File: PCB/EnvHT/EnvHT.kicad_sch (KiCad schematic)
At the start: 21 parts, among them J1 DC, J2 DC, J4 Shelly, U1 LMR16006XDDCR, U4 ESP32-PICO-MINI-02, U7 SHT40

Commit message: Library update
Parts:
- added C5: 10nF, RevK:C_0603, symbol Device:C
- added S1, S2: Screw, RevK:Screw, symbol RevK:Screw
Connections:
- net GND: now also C5.1
- net at R12.2, U4.8 (EN): now also C5.2
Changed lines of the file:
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@@
   (junction (at 197.485 41.275) (diameter 0) (color 0 0 0 0)
+  )
+  (junction (at 40.64 31.75) (diameter 0) (color 0 0 0 0)
   )
   (junction (at 73.66 38.1) (diameter 0) (color 0 0 0 0)
@@
     (pin "1")
     (pin "2")
+  )
+  (symbol (lib_id "Device:C") (at 36.83 31.75 90) (unit 1)
+    (in_bom yes) (on_board yes) (fields_autoplaced)
+    (property "Reference" "C5" (id 0) (at 36.83 25.8912 90))
+    (property "Value" "10nF" (id 1) (at 36.83 28.4281 90))
+    (property "Footprint" "RevK:C_0603" (id 2) (at 40.64 30.7848 0)
+      (effects (font (size 1.27 1.27)) hide)
+    )
+    (property "Datasheet" "~" (id 3) (at 36.83 31.75 0)
+      (effects (font (size 1.27 1.27)) hide)
+    )
+    (pin "1")
+    (pin "2")
+  )
+  (symbol (lib_name "Screw_1") (lib_id "RevK:Screw") (at 266.7 170.18 0) (unit 1)
+    (in_bom no) (on_board yes) (fields_autoplaced)
+    (property "Reference" "S1" (id 0) (at 268.3092 169.3453 0)
+      (effects (font (size 1.27 1.27)) (justify left))
+    )
+    (property "Value" "Screw" (id 1) (at 268.3092 171.8822 0)
+      (effects (font (size 1.27 1.27)) (justify left))
+    )
+    (property "Footprint" "RevK:Screw" (id 2) (at 266.7 170.18 0)
+      (effects (font (size 1.27 1.27)) hide)
+    )
+    (property "Datasheet" "" (id 3) (at 266.7 170.18 0)
+      (effects (font (size 1.27 1.27)) hide)
+    )
   )
   (symbol (lib_id "RevK:Shelly") (at 73.66 40.64 0) (unit 1)
@@
     (pin "2")
   )
+  (symbol (lib_id "power:GND") (at 33.02 31.75 270) (unit 1)
+    (in_bom yes) (on_board yes)
+    (property "Reference" "#PWR0104" (id 0) (at 26.67 31.75 0)
+      (effects (font (size 1.27 1.27)) hide)
+    )
+    (property "Value" "GND" (id 1) (at 29.21 35.56 90)
+      (effects (font (size 1.27 1.27)) (justify left))
+    )
+    (property "Footprint" "" (id 2) (at 33.02 31.75 0)
+      (effects (font (size 1.27 1.27)) hide)
+    )
+    (property "Datasheet" "" (id 3) (at 33.02 31.75 0)
+      (effects (font (size 1.27 1.27)) hide)
+    )
+    (pin "1")
+  )
   (symbol (lib_id "Device:R") (at 201.295 46.99 90) (unit 1)
     (in_bom yes) (on_board yes)
@@
     (pin "1")
   )
+  (symbol (lib_id "RevK:Screw") (at 271.78 170.18 0) (unit 1)
+    (in_bom no) (on_board yes) (fields_autoplaced)
+    (property "Reference" "S2" (id 0) (at 273.3892 169.3453 0)
+      (effects (font (size 1.27 1.27)) (justify left))
+    )
+    (property "Value" "Screw" (id 1) (at 273.3892 171.8822 0)
+      (effects (font (size 1.27 1.27)) (justify left))
+    )
+    (property "Footprint" "RevK:Screw" (id 2) (at 271.78 170.18 0)
+      (effects (font (size 1.27 1.27)) hide)
+    )
+    (property "Datasheet" "" (id 3) (at 271.78 170.18 0)
+      (effects (font (size 1.27 1.27)) hide)
+    )
+  )
   (sheet_instances
     (path "/" (page "1"))
@@
       (reference "#PWR0103") (unit 1) (value "GND") (footprint "")
     )
+    (path "/ab4a0c90-0985-4f7f-ab2f-82b6932ae924"
+      (reference "#PWR0104") (unit 1) (value "GND") (footprint "")
+    )
     (path "/78b9a69e-c8d1-4e40-b0f1-df5a0164aa20"
       (reference "#PWR0106") (unit 1) (value "GND") (footprint "")
@@
       (reference "C4") (unit 1) (value "100nF") (footprint "RevK:C_0603")
     )
+    (path "/0c39c12b-6289-4e50-be09-f571fe888dab"
+      (reference "C5") (unit 1) (value "10nF") (footprint "RevK:C_0603")
+    )
     (path "/6317ccc8-6edd-48eb-98c0-5a7f98d8bfba"
       (reference "D1") (unit 1) (value "Schottky") (footprint "RevK:D_1206_")
@@
       (reference "R12") (unit 1) (value "10k") (footprint "RevK:R_0603")
     )
+    (path "/103a99a3-9383-4e45-b6ef-eeffc7751b9d"
+      (reference "S1") (unit 1) (value "Screw") (footprint "RevK:Screw")
+    )
+    (path "/d5746733-9963-4338-b10b-19507460e17d"
+      (reference "S2") (unit 1) (value "Screw") (footprint "RevK:Screw")
+    )
     (path "/49fac067-22c4-46c0-be10-03a6c28d472f"

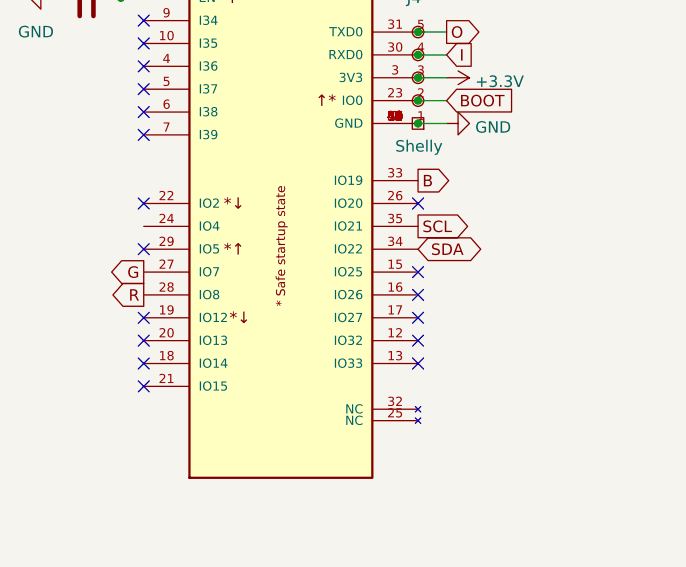
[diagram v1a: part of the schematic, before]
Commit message: Tracked EnvHT
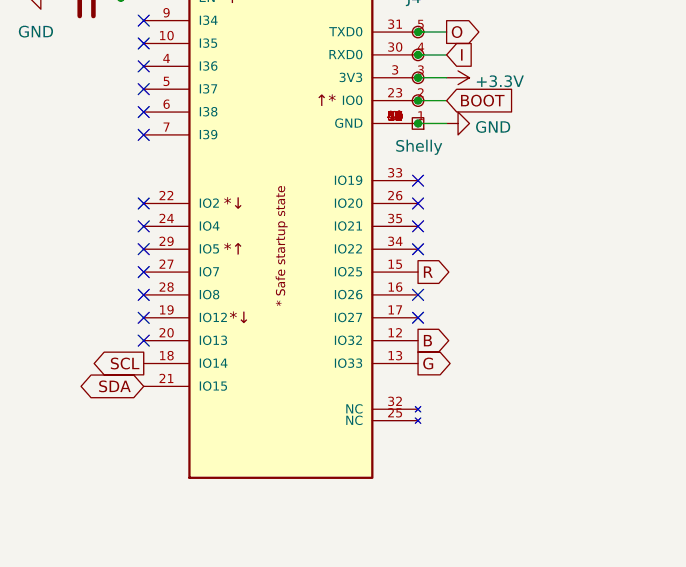
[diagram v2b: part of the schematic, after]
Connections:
- net B: now also U4.12 (IO32); no longer U4.33 (IO19)
- net G: now also U4.13 (IO33); no longer U4.27 (IO7)
- net R: now also U4.15 (IO25); no longer U4.28 (IO8)
- net SCL: now also U4.18 (IO14); no longer U4.35 (IO21)
- net SDA: now also U4.21 (IO15); no longer U4.34 (IO22)
- no-connect marks 18 -> 19
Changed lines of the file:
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@@
   (no_connect (at 73.66 64.77))
   (no_connect (at 43.18 69.85))
-  (no_connect (at 73.66 62.23))
+  (no_connect (at 43.18 64.77))
   (no_connect (at 43.18 59.69))
   (no_connect (at 73.66 54.61))
-  (no_connect (at 73.66 69.85))
-  (no_connect (at 43.18 74.93))
+  (no_connect (at 73.66 52.07))
+  (no_connect (at 73.66 59.69))
   (no_connect (at 43.18 44.45))
   (no_connect (at 43.18 46.99))
@@
   (no_connect (at 73.66 67.31))
   (no_connect (at 43.18 67.31))
-  (no_connect (at 73.66 72.39))
-  (no_connect (at 43.18 72.39))
+  (no_connect (at 43.18 57.15))
+  (no_connect (at 43.18 62.23))
+  (no_connect (at 73.66 57.15))
   (wire (pts (xy 194.945 38.735) (xy 205.105 38.735))
     (stroke (width 0) (type default) (color 0 0 0 0))
@@
     (stroke (width 0) (type default) (color 0 0 0 0))
   )
-  (global_label "B" (shape output) (at 73.66 52.07 0) (fields_autoplaced)
+  (global_label "B" (shape output) (at 73.66 69.85 0) (fields_autoplaced)
     (effects (font (size 1.27 1.27)) (justify left))
-    (property "Intersheet References" "${INTERSHEET_REFS}" (id 0) (at 77.2542 52.1494 0)
+    (property "Intersheet References" "${INTERSHEET_REFS}" (id 0) (at 77.2542 69.9294 0)
       (effects (font (size 1.27 1.27)) (justify left) hide)
     )
@@
     )
   )
-  (global_label "SCL" (shape output) (at 73.66 57.15 0) (fields_autoplaced)
-    (effects (font (size 1.27 1.27)) (justify left))
-    (property "Intersheet References" "${INTERSHEET_REFS}" (id 0) (at 79.4918 57.0706 0)
-      (effects (font (size 1.27 1.27)) (justify left) hide)
+  (global_label "SCL" (shape output) (at 43.18 72.39 180) (fields_autoplaced)
+    (effects (font (size 1.27 1.27)) (justify right))
+    (property "Intersheet References" "${INTERSHEET_REFS}" (id 0) (at 37.3482 72.4694 0)
+      (effects (font (size 1.27 1.27)) (justify right) hide)
     )
   )
@@
     )
   )
-  (global_label "R" (shape output) (at 43.18 64.77 180) (fields_autoplaced)
-    (effects (font (size 1.27 1.27)) (justify right))
-    (property "Intersheet References" "${INTERSHEET_REFS}" (id 0) (at 39.5858 64.6906 0)
-      (effects (font (size 1.27 1.27)) (justify right) hide)
+  (global_label "R" (shape output) (at 73.66 62.23 0) (fields_autoplaced)
+    (effects (font (size 1.27 1.27)) (justify left))
+    (property "Intersheet References" "${INTERSHEET_REFS}" (id 0) (at 77.2542 62.3094 0)
+      (effects (font (size 1.27 1.27)) (justify left) hide)
     )
   )
-  (global_label "G" (shape output) (at 43.18 62.23 180) (fields_autoplaced)
-    (effects (font (size 1.27 1.27)) (justify right))
-    (property "Intersheet References" "${INTERSHEET_REFS}" (id 0) (at 39.5858 62.3094 0)
-      (effects (font (size 1.27 1.27)) (justify right) hide)
+  (global_label "G" (shape output) (at 73.66 72.39 0) (fields_autoplaced)
+    (effects (font (size 1.27 1.27)) (justify left))
+    (property "Intersheet References" "${INTERSHEET_REFS}" (id 0) (at 77.2542 72.3106 0)
+      (effects (font (size 1.27 1.27)) (justify left) hide)
     )
   )
@@
     )
   )
-  (global_label "SDA" (shape bidirectional) (at 73.66 59.69 0) (fields_autoplaced)
-    (effects (font (size 1.27 1.27)) (justify left))
-    (property "Intersheet References" "${INTERSHEET_REFS}" (id 0) (at 79.5523 59.6106 0)
-      (effects (font (size 1.27 1.27)) (justify left) hide)
+  (global_label "SDA" (shape bidirectional) (at 43.18 74.93 180) (fields_autoplaced)
+    (effects (font (size 1.27 1.27)) (justify right))
+    (property "Intersheet References" "${INTERSHEET_REFS}" (id 0) (at 37.2877 75.0094 0)
+      (effects (font (size 1.27 1.27)) (justify right) hide)
     )
   )

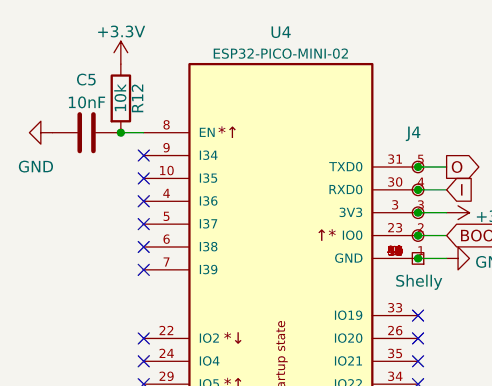
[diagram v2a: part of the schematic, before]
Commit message: Cap chanmge
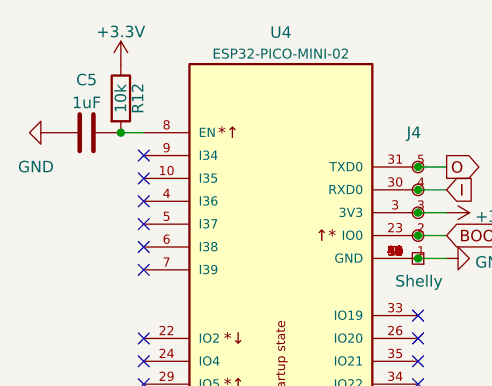
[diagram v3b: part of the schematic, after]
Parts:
- C5: value 10nF -> 1uF
- J1, J2: footprint RevK:PTSM-HH-2-RA -> RevK:PTSM-HH1-2-RA

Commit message: Tidy
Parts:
- added U2: QR, RevK:QR-ENVMON, symbol RevK:QR
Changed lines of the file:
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@@
   (title_block
     (title "Simple Humidity / Temp sensor 12V")
-    (date "${DATE}")
     (rev "1")
     (company "Adrian Kennard / Andrews & Arnold Ltd")
@@
         )
       )
+    )
+  )
+  (symbol (lib_id "RevK:QR") (at 261.366 170.18 0) (unit 1)
+    (in_bom no) (on_board yes) (dnp no) (fields_autoplaced)
+    (property "Reference" "U2" (at 261.366 173.355 0)
+      (effects (font (size 1.27 1.27)) hide)
+    )
+    (property "Value" "QR" (at 261.366 173.355 0)
+      (effects (font (size 1.27 1.27)) hide)
+    )
+    (property "Footprint" "RevK:QR-ENVMON" (at 260.731 170.815 0)
+      (effects (font (size 1.27 1.27)) hide)
+    )
+    (property "Datasheet" "" (at 260.731 170.815 0)
+      (effects (font (size 1.27 1.27)) hide)
+    )
+    (property "Note" "Non part, PCB printed" (at 261.366 170.18 0)
+      (effects (font (size 1.27 1.27)) hide)
+    )
+    (instances
+      (project "EnvHT"
+        (path "/12422a89-3d0c-485c-9386-f77121fd68fd"
+          (reference "U2") (unit 1)
+        )
+      )

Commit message: Library update
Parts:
- removed C1: 100nF, RevK:C_0603_, symbol RevK:Hidden
- removed C2: 2.2uF, RevK:C_0805_, symbol RevK:Hidden
- removed C3: 10uF, RevK:C_0805_, symbol RevK:Hidden
- removed C5: 1uF, RevK:C_0603, symbol Device:C
- removed D1: Schottky, RevK:D_1206_, symbol RevK:Hidden
- removed D2: D, RevK:D_1206, symbol Device:D
- removed D3: LED_BARG, RevK:MHS190RGBCT, symbol Device:LED_BARG
- removed J4: Shelly, RevK:Shelly, symbol RevK:Shelly
- removed L1: 6.8uH, RevK:L_4x4_, symbol RevK:Hidden
- removed R12: 10k, RevK:R_0603, symbol Device:R
- removed R2: 30k 1%, RevK:R_0603, symbol Device:R
- removed R7: 300R, RevK:R_0603, symbol Device:R
- removed R8: 1K, RevK:R_0603, symbol Device:R
- removed R9: 100R, RevK:R_0603, symbol Device:R
- removed U1: LMR16006XDDCR, RevK:SOT-23-Thin-6-Reg, symbol RevK:LMR16006XDDCR
- removed U2: QR, RevK:QR-ENVMON, symbol RevK:QR
- removed U4: ESP32-PICO-MINI-02, RevK:ESP32-PICO-MINI-02, symbol RevK:ESP32-PICO-MINI-02
- added C1: 100nF, RevK:C_0402, symbol Device:C
- added C2: 22uF, RevK:C_0603, symbol Device:C
- added C3: 1uF, RevK:C_0402, symbol Device:C
- added C6: 10uF 50V, RevK:C_0603_, symbol RevK:Hidden
- added C7: 10uF 6.3V, RevK:C_0603_, symbol RevK:Hidden
- added C8: 100nF, RevK:C_0603_, symbol RevK:Hidden
- added D1: D, RevK:D_SOD-123, symbol Device:D
- added D4: RGB, RevK:LED-RGB-1.6x1.6, symbol Device:LED_RGBA
- added J3: Shelly, RevK:Shelly, symbol RevK:Shelly
- added J4: USB-PROG, RevK:USB-PROG, symbol RevK:USB-PROG
- added L2: 10uH, RevK:L_4x4_, symbol RevK:Hidden
- added R3: 680R, RevK:R_0402, symbol Device:R
- added R4: 2K, RevK:R_0402, symbol Device:R
- added R5: 220R, RevK:R_0402, symbol Device:R
- added R6: 124k, RevK:R_0402_, symbol RevK:Hidden
- added R7: 39k2, RevK:R_0402_, symbol RevK:Hidden
- added R8: 1M, RevK:R_0402_, symbol RevK:Hidden
- added U1: ESP32-S3-MINI-1, RevK:ESP32-S3-MINI-1, symbol RevK:ESP32-S3-MINI-1-N4R2
- added U3: MD8942, RevK:SOT-23-6-MD8942, symbol RevK:MD89420-RegBlock
- C4: footprint RevK:C_0603 -> RevK:C_0402
- R1: value 100k 1% -> 10K; footprint RevK:R_0603 -> RevK:R_0402; LCSC Part # C14675 -> (none)
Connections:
- net +3.3V: now also C1.1, C2.1, D4.4 (A), J3.3 (3V3), U1.3 (3V3), U3.8 (VOUT)
- net B: now also R5.2, U1.10 (GPIO6)
- net DC: now also D1.1 (K), J4.1 (VBUS), U3.5 (VIN)
- net G: now also R4.2, U1.8 (GPIO4)
- net GND: now also C1.2, C2.2, C3.2, J3.1 (GND), J4.4 (GND), U1.1 (GND), U1.13 (GPIO9), U1.14 (GPIO10), U1.2 (GND), U1.42 (GND), U1.43 (GND), U1.44 (GPIO46), U1.46 (GND), U1.47 (GND), U1.48 (GND), U1.49 (GND), U1.50 (GND), U1.51 (GND), U1.52 (GND), U1.53 (GND), U1.54 (GND), U1.55 (GND), U1.56 (GND), U1.57 (GND), U1.58 (GND), U1.59 (GND), U1.60 (GND), U1.61 (GND), U1.62 (GND), U1.63 (GND), U1.64 (GND), U1.65 (GND), U1.7 (GPIO3), U3.2 (GND), U3.7 (GND)
- net R: now also R3.2, U1.9 (GPIO5)
- net SCL: now also U1.31 (GPIO35)
- net SDA: now also U1.32 (GPIO36)
- net at J1.2 (DC), J2.2 (DC): now also D1.2 (A)
- net at R1.2: now also C3.1, U1.45 (EN)
- new net: J3.2 (0), U1.4 (GPIO0)
- new net: J3.4 (Rx), U1.40 (GPIO44)
- new net: J3.5 (Tx), U1.39 (GPIO43)
- new net: D4.3 (BK), R5.1
- new net: D4.1 (RK), R3.1
- new net: D4.2 (GK), R4.1
- new net D+: J4.3 (D+), U1.24 (GPIO20)
- new net D-: J4.2 (D-), U1.23 (GPIO19)
- no-connect marks 19 -> 1

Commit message: Library update
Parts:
- removed Logo1: AJK, RevK:AJK, symbol RevK:AJK
- added PCB1: 70x70, RevK:PCB7070, symbol RevK:PCB
- added V2, V3: ~, RevK:VCUT70, symbol RevK:VCUT
- J1, J2: now left out of the parts list
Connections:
- net GND: now also U1.11 (GPIO7), U1.12 (GPIO8), U1.15 (GPIO11), U1.5 (GPIO1), U1.6 (GPIO2)
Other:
- moved on the sheet: S1, S2

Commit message: PCB Update
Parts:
- C6: LCSC Part # C1591 -> (none); MPN (none) -> C1591
- C7: LCSC Part # C1691 -> (none); MPN (none) -> C1691
- D1: LCSC Part # C1884542 -> (none); MPN (none) -> C1884542
- D4: LCSC Part # C264508 -> (none); MPN (none) -> C264508
- U1: LCSC Part # C3013941 -> (none); MPN (none) -> C3013941
- U3: LCSC Part # C2684786 -> (none); MPN (none) -> C2684786
- U7: LCSC Part # C2909890 -> (none); MPN (none) -> C2909890
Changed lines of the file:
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@@
       (effects (font (size 1.27 1.27)) hide)
     )
-    (property "LCSC Part #" "C1591" (at 144.145 122.555 0)
+    (property "MPN" "C1591" (at 144.145 122.555 0)
       (effects (font (size 1.27 1.27)) hide)
     )
@@
       (effects (font (size 1.27 1.27)) (justify left bottom) hide)
     )
-    (property "LCSC Part #" "C3013941" (at 55.245 118.11 0)
+    (property "MPN" "C3013941" (at 55.245 118.11 0)
       (effects (font (size 1.27 1.27)) hide)
     )
@@
       (effects (font (size 1.27 1.27)) hide)
     )
-    (property "LCSC Part #" "C1884542" (at 109.22 29.21 0)
+    (property "MPN" "C1884542" (at 109.22 29.21 0)
       (effects (font (size 1.27 1.27)) hide)
     )
@@
       (effects (font (size 1.27 1.27)) hide)
     )
-    (property "LCSC Part #" "C264508" (at 125.095 96.52 0)
+    (property "MPN" "C264508" (at 125.095 96.52 0)
       (effects (font (size 1.27 1.27)) hide)
     )
@@
       (effects (font (size 1.27 1.27)) (justify left) hide)
     )
-    (property "LCSC Part #" "C2909890" (at 125.222 65.2007 0)
+    (property "MPN" "C2909890" (at 125.222 65.2007 0)
       (effects (font (size 1.27 1.27)) (justify left) hide)
     )
@@
       (effects (font (size 1.27 1.27)) hide)
     )
-    (property "LCSC Part #" "C1691" (at 144.145 124.46 0)
+    (property "MPN" "C1691" (at 144.145 124.46 0)
       (effects (font (size 1.27 1.27)) hide)
     )
@@
       (effects (font (size 1.27 1.27)) hide)
     )
-    (property "LCSC Part #" "C2684786" (at 123.19 155.575 0)
-      (effects (font (size 1.27 1.27)) hide)
-    )
+    (property "MPN" "C2684786" (at 123.19 155.575 0)
+      (effects (font (size 1.27 1.27)) hide)
+    )
